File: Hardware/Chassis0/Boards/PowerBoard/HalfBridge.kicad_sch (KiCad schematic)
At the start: 10 parts, among them Q1 IPB017N10N5ATMA1, Q2 IPB017N10N5ATMA1, Q3 IPB017N10N5ATMA1, Q4 IPB017N10N5ATMA1

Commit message: Update chassis 0 gate driver board, remove old files
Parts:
- added D12: BAT54WS-7-F, InverterCom:SOD2513X120N, symbol InverterCom:BAT54WS-7-F
- added R68: 9.1, Resistor_SMD:R_1210_3225Metric_Pad1.30x2.65mm_HandSolder, symbol Device:R
- added R69: 6.8, Resistor_SMD:R_1210_3225Metric_Pad1.30x2.65mm_HandSolder, symbol Device:R
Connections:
- new net: D12.1 (K), R68.2
- new net: D12.2 (A), R69.2
- new net: R68.1, R69.1

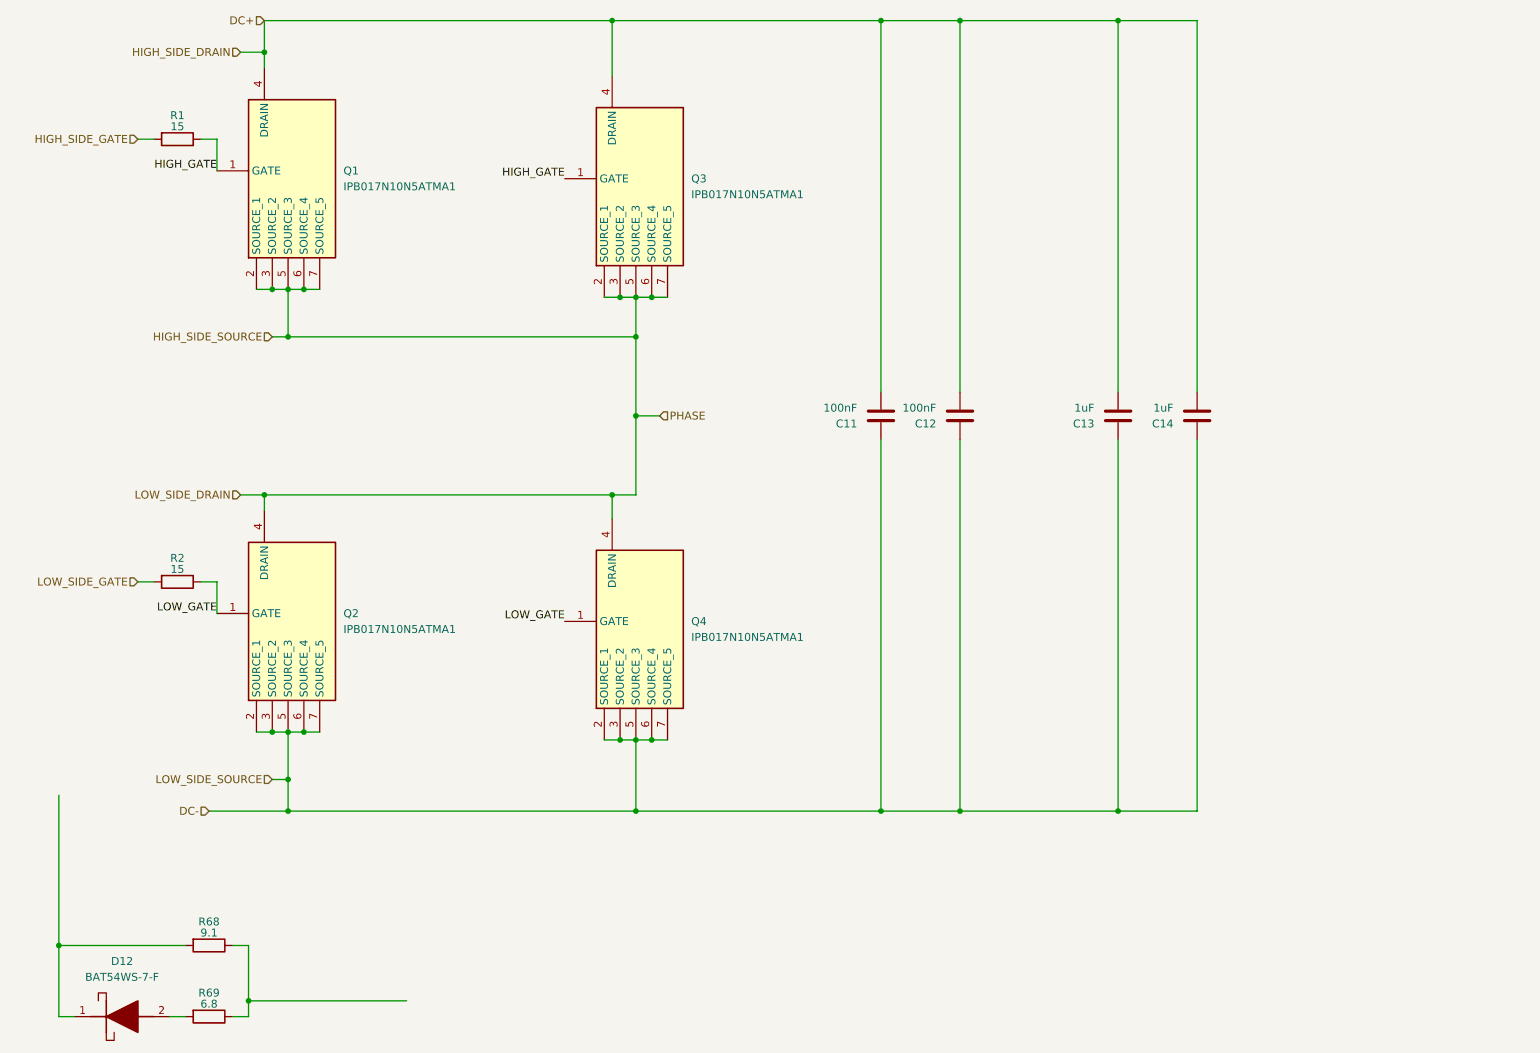
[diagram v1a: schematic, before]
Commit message: Add control board outline for size 0
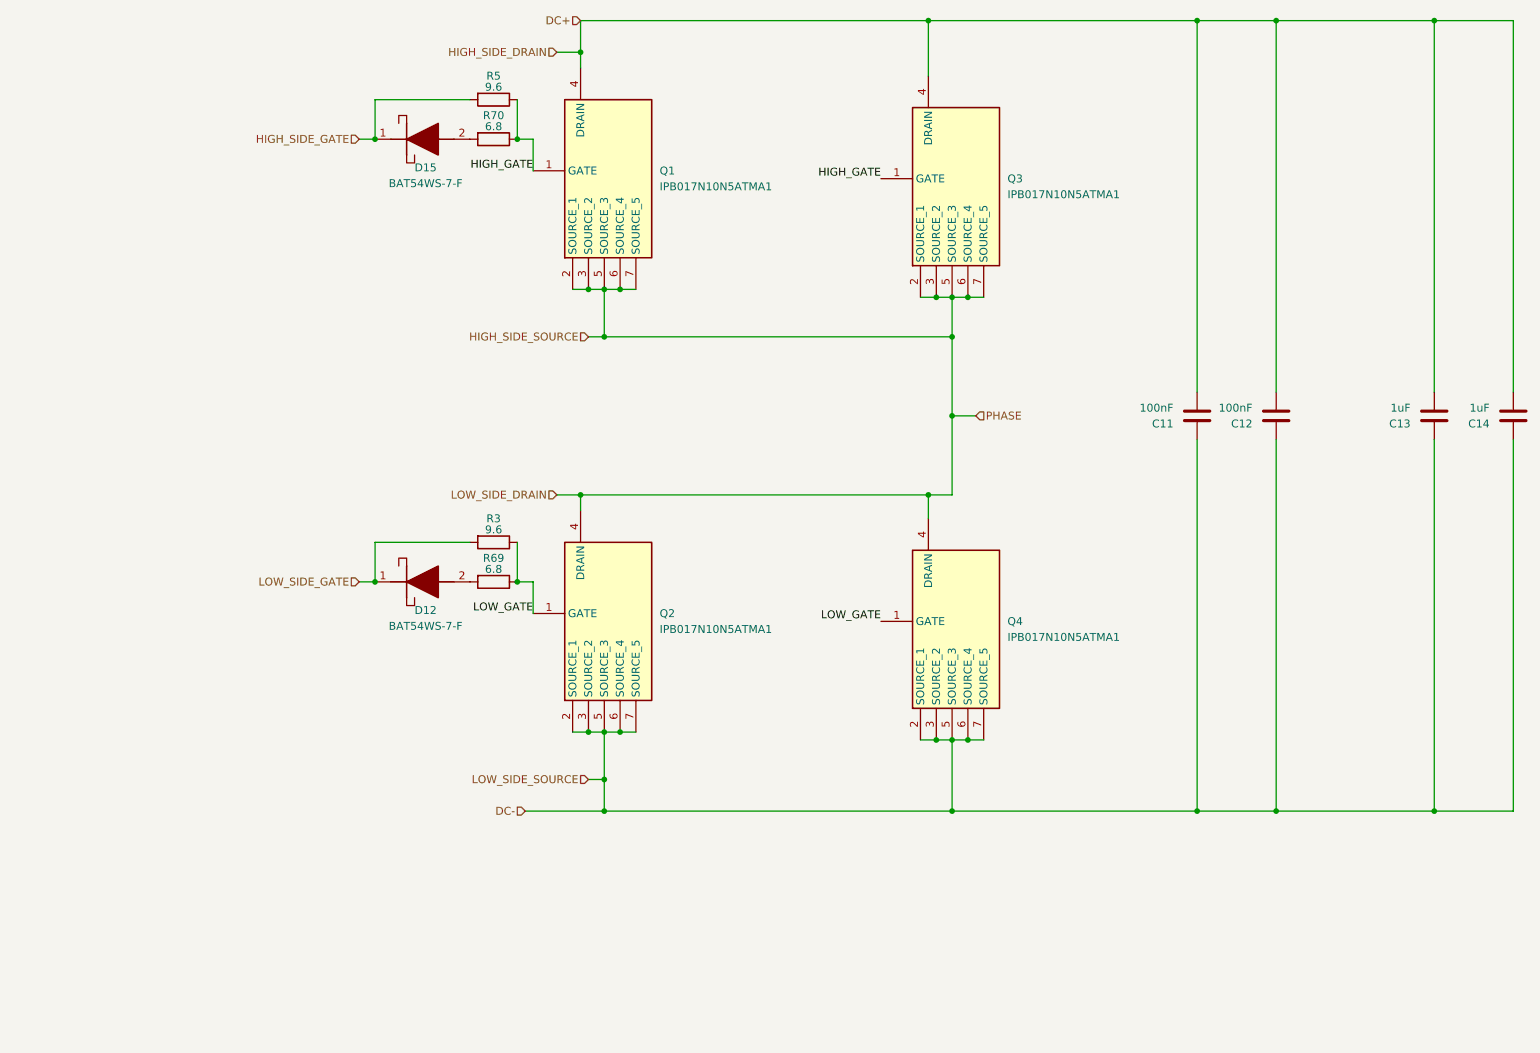
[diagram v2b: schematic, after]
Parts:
- removed R1, R2: 15, Resistor_SMD:R_1210_3225Metric_Pad1.30x2.65mm_HandSolder, symbol Device:R
- removed R68: 9.1, Resistor_SMD:R_1210_3225Metric_Pad1.30x2.65mm_HandSolder, symbol Device:R
- added D15: BAT54WS-7-F, InverterCom:SOD2513X120N, symbol InverterCom:BAT54WS-7-F
- added R3, R5: 9.6, Resistor_SMD:R_1210_3225Metric_Pad1.30x2.65mm_HandSolder, symbol Device:R
- added R70: 6.8, Resistor_SMD:R_1210_3225Metric_Pad1.30x2.65mm_HandSolder, symbol Device:R
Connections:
- net HIGH_GATE: now also R5.1, R70.1
- net HIGH_SIDE_GATE: now also D15.1 (K), R5.2
- net LOW_GATE: now also R69.1, R3.1
- net LOW_SIDE_GATE: now also D12.1 (K), R3.2
- new net: D15.2 (A), R70.2
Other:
- moved on the sheet: C11, C12, C13, C14, D12, Q1, Q2, Q3, Q4, R69
